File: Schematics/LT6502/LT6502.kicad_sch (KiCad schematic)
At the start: 38 parts, among them U1 TC1232, U2 W65C02S6TQG-14, U3 IS62C256AL, U4 IS62C256AL, U5 SST39SF010

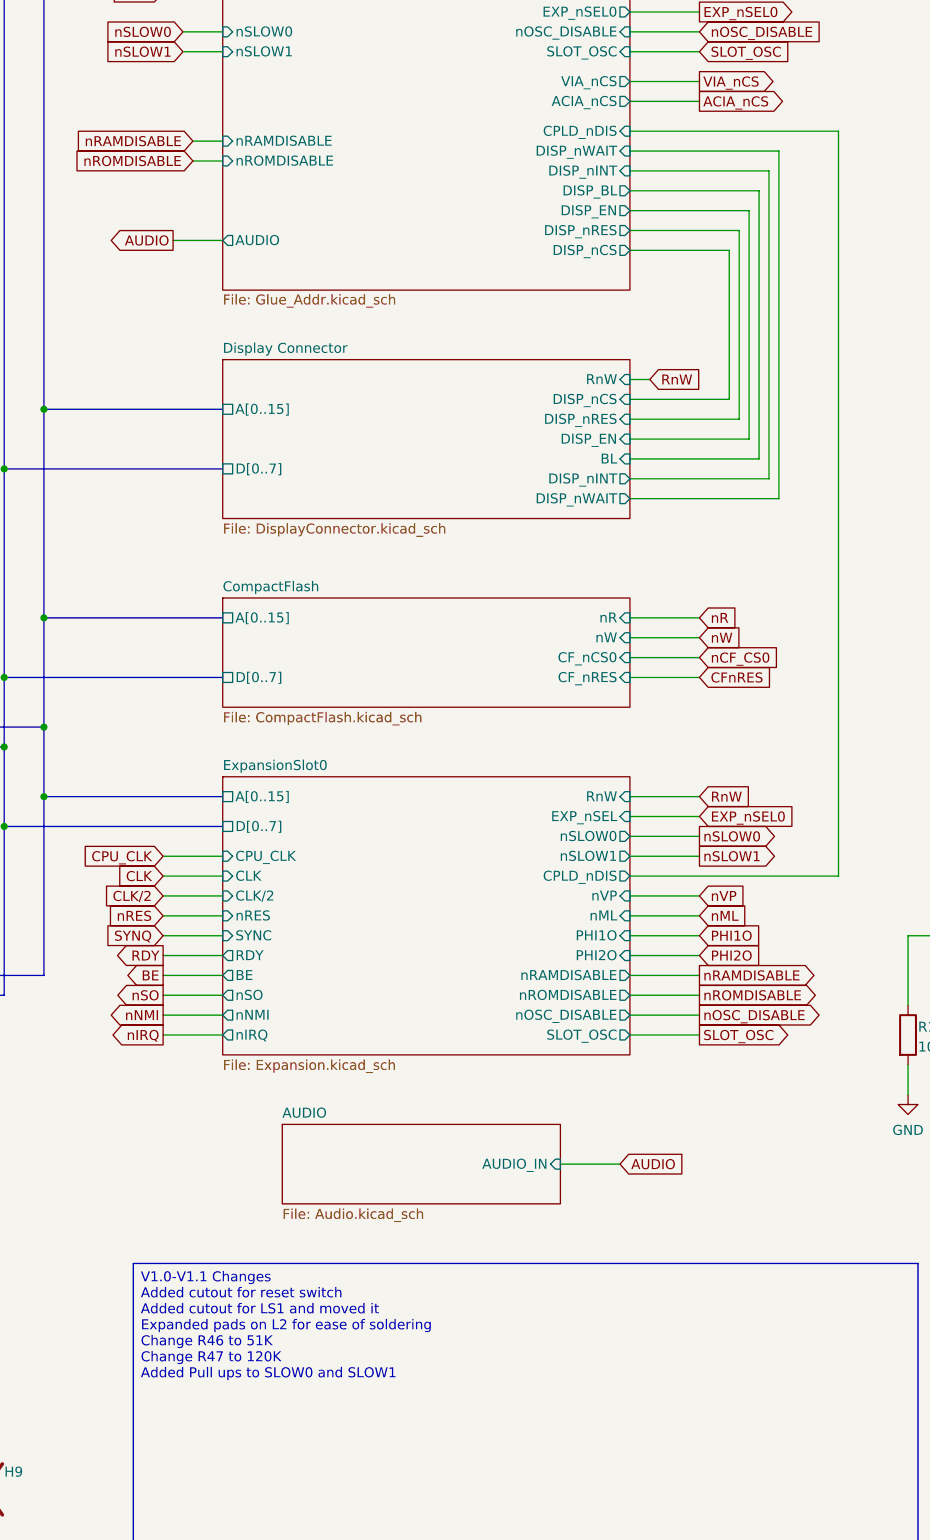
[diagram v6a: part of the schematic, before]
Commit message: Added enable for TXS0108 on data bus
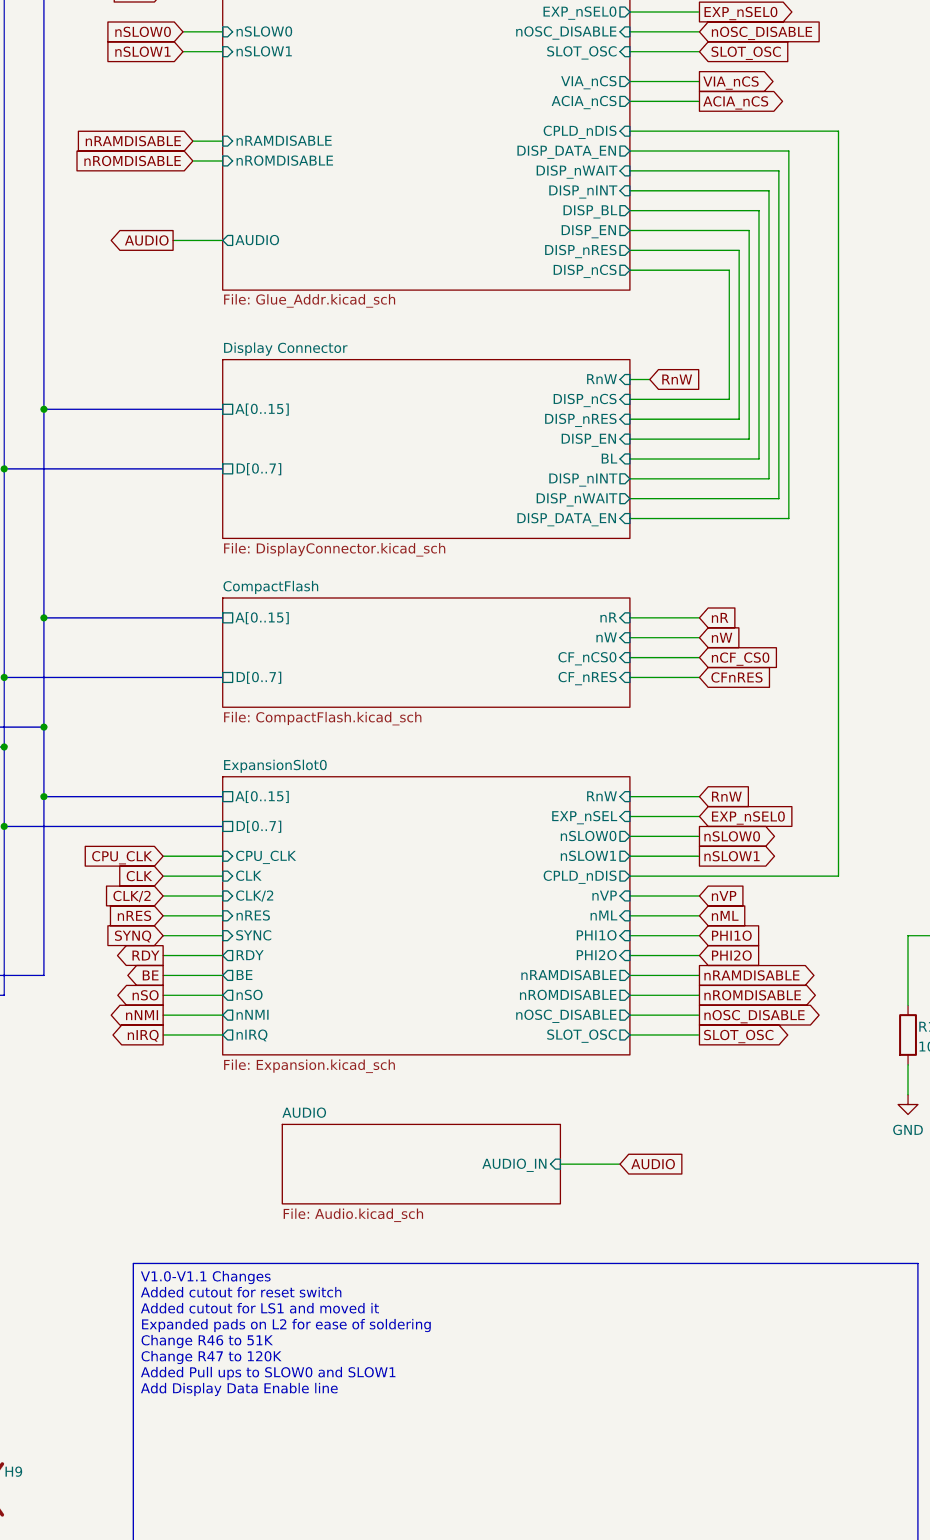
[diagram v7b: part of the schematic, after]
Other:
- sheet Display Connector ports: added DISP_DATA_EN; removed none
- sheet Glue_Addr ports: added DISP_DATA_EN; removed none
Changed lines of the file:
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@@
 		)
 	)
-	(text_box "V1.0-V1.1 Changes\nAdded cutout for reset switch\nAdded cutout for LS1 and moved it\nExpanded pads on L2 for ease of soldering\nChange R46 to 51K\nChange R47 to 120K\nAdded Pull ups to SLOW0 and SLOW1"
+	(text_box "V1.0-V1.1 Changes\nAdded cutout for reset switch\nAdded cutout for LS1 and moved it\nExpanded pads on L2 for ease of soldering\nChange R46 to 51K\nChange R47 to 120K\nAdded Pull ups to SLOW0 and SLOW1\nAdd Display Data Enable line"
 		(exclude_from_sim no)
 		(at 179.07 238.76 0)
@@
 	(wire
 		(pts
-			(xy 242.57 109.22) (xy 255.27 109.22)
+			(xy 242.57 111.76) (xy 255.27 111.76)
 		)
 		(stroke
@@
 	(wire
 		(pts
-			(xy 260.35 99.06) (xy 260.35 138.43)
+			(xy 260.35 101.6) (xy 260.35 138.43)
 		)
 		(stroke
@@
 	(wire
 		(pts
-			(xy 261.62 96.52) (xy 261.62 140.97)
+			(xy 261.62 99.06) (xy 261.62 140.97)
 		)
 		(stroke
@@
 	(wire
 		(pts
-			(xy 242.57 104.14) (xy 257.81 104.14)
+			(xy 242.57 106.68) (xy 257.81 106.68)
 		)
 		(stroke
@@
 	(wire
 		(pts
-			(xy 242.57 96.52) (xy 261.62 96.52)
+			(xy 242.57 99.06) (xy 261.62 99.06)
 		)
 		(stroke
@@
 	(wire
 		(pts
+			(xy 242.57 96.52) (xy 262.89 96.52)
+		)
+		(stroke
+			(width 0)
+			(type default)
+		)
+	)
+	(wire
+		(pts
 			(xy 111.76 105.41) (xy 39.37 105.41)
 		)
@@
 	(wire
 		(pts
-			(xy 242.57 101.6) (xy 259.08 101.6)
+			(xy 242.57 104.14) (xy 259.08 104.14)
 		)
 		(stroke
@@
 	(wire
 		(pts
+			(xy 262.89 96.52) (xy 262.89 143.51)
+		)
+		(stroke
+			(width 0)
+			(type default)
+		)
+	)
+	(wire
+		(pts
 			(xy 182.88 201.93) (xy 190.5 201.93)
 		)
@@
 	(wire
 		(pts
-			(xy 255.27 109.22) (xy 255.27 128.27)
+			(xy 255.27 111.76) (xy 255.27 128.27)
 		)
 		(stroke
@@
 	(wire
 		(pts
-			(xy 256.54 106.68) (xy 256.54 130.81)
+			(xy 256.54 109.22) (xy 256.54 130.81)
 		)
 		(stroke
@@
 	(wire
 		(pts
-			(xy 257.81 104.14) (xy 257.81 133.35)
+			(xy 257.81 106.68) (xy 257.81 133.35)
 		)
 		(stroke
@@
 	(wire
 		(pts
-			(xy 242.57 106.68) (xy 256.54 106.68)
+			(xy 242.57 109.22) (xy 256.54 109.22)
 		)
 		(stroke
@@
 	(wire
 		(pts
-			(xy 259.08 101.6) (xy 259.08 135.89)
+			(xy 259.08 104.14) (xy 259.08 135.89)
 		)
 		(stroke
@@
 	(wire
 		(pts
+			(xy 262.89 143.51) (xy 242.57 143.51)
+		)
+		(stroke
+			(width 0)
+			(type default)
+		)
+	)
+	(wire
+		(pts
 			(xy 316.23 53.34) (xy 306.07 53.34)
 		)
@@
 	(wire
 		(pts
-			(xy 242.57 99.06) (xy 260.35 99.06)
+			(xy 242.57 101.6) (xy 260.35 101.6)
 		)
 		(stroke
@@
 	(sheet
 		(at 190.5 123.19)
-		(size 52.07 20.32)
+		(size 52.07 22.86)
 		(exclude_from_sim no)
 		(in_bom yes)
@@
 		)
 		(property "Sheetfile" "DisplayConnector.kicad_sch"
-			(at 190.5 144.0946 0)
+			(at 190.5 146.6346 0)
 			(effects
 				(font
@@
 			)
 		)
+		(pin "DISP_DATA_EN" input
+			(at 242.57 143.51 0)
+			(effects
+				(font
+					(size 1.27 1.27)
+				)
+				(justify right)
+			)
+		)
 		(instances
 			(project "LT6502"
@@
 		)
 		(pin "DISP_EN" output
-			(at 242.57 104.14 0)
+			(at 242.57 106.68 0)
 			(effects
 				(font
@@
 		)
 		(pin "DISP_nCS" output
-			(at 242.57 109.22 0)
+			(at 242.57 111.76 0)
 			(effects
 				(font
@@
 		)
 		(pin "DISP_nWAIT" input
-			(at 242.57 96.52 0)
+			(at 242.57 99.06 0)
 			(effects
 				(font
@@
 		)
 		(pin "DISP_nINT" input
-			(at 242.57 99.06 0)
+			(at 242.57 101.6 0)
 			(effects
 				(font
@@
 		)
 		(pin "DISP_nRES" output
-			(at 242.57 106.68 0)
+			(at 242.57 109.22 0)
 			(effects
 				(font
@@
 		)
 		(pin "DISP_BL" output
-			(at 242.57 101.6 0)
+			(at 242.57 104.14 0)
 			(effects
 				(font
@@
 			)
 		)
+		(pin "DISP_DATA_EN" output
+			(at 242.57 96.52 0)
+			(effects
+				(font
+					(size 1.27 1.27)
+				)
+				(justify right)
+			)
+		)
